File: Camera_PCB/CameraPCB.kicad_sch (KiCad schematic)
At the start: 0 parts

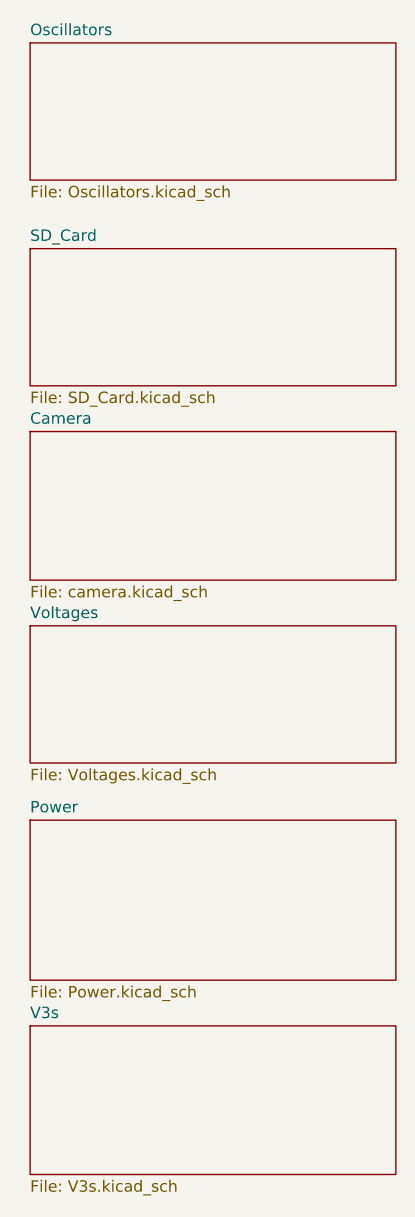
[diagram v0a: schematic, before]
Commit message: 10/29 Footprint Additions
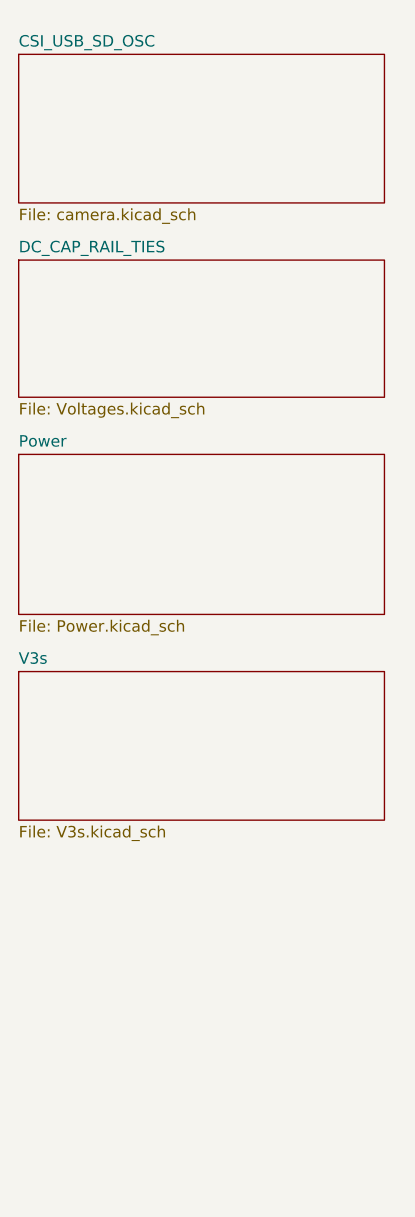
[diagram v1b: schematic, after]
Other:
- sheet Camera renamed CSI_USB_SD_OSC
- sheet Voltages renamed DC_CAP_RAIL_TIES
- removed sheet Oscillators
- removed sheet SD_Card
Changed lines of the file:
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@@
 	)
 	(sheet
-		(at 17.78 60.96)
+		(at 16.51 19.05)
 		(size 40.64 16.51)
 		(exclude_from_sim no)
@@
 			(color 0 0 0 0.0000)
 		)
-		(property "Sheetname" "Camera"
-			(at 17.78 60.2484 0)
+		(property "Sheetname" "CSI_USB_SD_OSC"
+			(at 16.51 18.3384 0)
 			(effects
 				(font
@@
 		)
 		(property "Sheetfile" "camera.kicad_sch"
-			(at 17.78 78.0546 0)
+			(at 16.51 36.1446 0)
 			(effects
 				(font
@@
 	)
 	(sheet
-		(at 17.78 127)
+		(at 16.51 87.63)
 		(size 40.64 16.51)
 		(exclude_from_sim no)
@@
 		)
 		(property "Sheetname" "V3s"
-			(at 17.78 126.2884 0)
+			(at 16.51 86.9184 0)
 			(effects
 				(font
@@
 		)
 		(property "Sheetfile" "V3s.kicad_sch"
-			(at 17.78 144.0946 0)
+			(at 16.51 104.7246 0)
 			(effects
 				(font
@@
 	)
 	(sheet
-		(at 17.78 17.78)
-		(size 40.64 15.24)
-		(exclude_from_sim no)
-		(in_bom yes)
-		(on_board yes)
-		(dnp no)
-		(fields_autoplaced yes)
-		(stroke
-			(width 0.1524)
-			(type solid)
-		)
-		(fill
-			(color 0 0 0 0.0000)
-		)
-		(property "Sheetname" "Oscillators"
-			(at 17.78 17.0684 0)
-			(effects
-				(font
-					(size 1.27 1.27)
-				)
-				(justify left bottom)
-			)
-		)
-		(property "Sheetfile" "Oscillators.kicad_sch"
-			(at 17.78 33.6046 0)
-			(effects
-				(font
-					(size 1.27 1.27)
-				)
-				(justify left top)
-			)
-		)
-		(instances
-			(project "CameraPCB"
-				(path "/400c1603-202c-4359-a830-d2f0d06dd3ce"
-					(page "2")
-				)
-			)
-		)
-	)
-	(sheet
-		(at 17.78 104.14)
+		(at 16.51 63.5)
 		(size 40.64 17.78)
 		(exclude_from_sim no)
@@
 		)
 		(property "Sheetname" "Power"
-			(at 17.78 103.4284 0)
+			(at 16.51 62.7884 0)
 			(effects
 				(font
@@
 		)
 		(property "Sheetfile" "Power.kicad_sch"
-			(at 17.78 122.5046 0)
+			(at 16.51 81.8646 0)
 			(effects
 				(font
@@
 	)
 	(sheet
-		(at 17.78 82.55)
+		(at 16.51 41.91)
 		(size 40.64 15.24)
 		(exclude_from_sim no)
@@
 			(color 0 0 0 0.0000)
 		)
-		(property "Sheetname" "Voltages"
-			(at 17.78 81.8384 0)
+		(property "Sheetname" "DC_CAP_RAIL_TIES"
+			(at 16.51 41.1984 0)
 			(effects
 				(font
@@
 		)
 		(property "Sheetfile" "Voltages.kicad_sch"
-			(at 17.78 98.3746 0)
+			(at 16.51 57.7346 0)
 			(effects
 				(font
@@
 				)
 			)
-		)
-	)
-	(sheet
-		(at 17.78 40.64)
-		(size 40.64 15.24)
-		(exclude_from_sim no)
-		(in_bom yes)
-		(on_board yes)
-		(dnp no)
-		(fields_autoplaced yes)
-		(stroke
-			(width 0.1524)
-			(type solid)
-		)
-		(fill
-			(color 0 0 0 0.0000)
-		)
-		(property "Sheetname" "SD_Card"
-			(at 17.78 39.9284 0)
-			(effects
-				(font
-					(size 1.27 1.27)
-				)
-				(justify left bottom)
-			)
-		)
-		(property "Sheetfile" "SD_Card.kicad_sch"
-			(at 17.78 56.4646 0)
-			(effects
-				(font
-					(size 1.27 1.27)
-				)
-				(justify left top)
-			)
-		)
-		(instances
-			(project "CameraPCB"
-				(path "/400c1603-202c-4359-a830-d2f0d06dd3ce"
-					(page "3")
-				)
-			)

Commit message: Camera PCB Schematic review 1
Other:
- sheet Power renamed AXP203
- added sheet 3V3_5V0 (untitled.kicad_sch)
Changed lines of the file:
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@@
 	)
 	(sheet
-		(at 16.51 87.63)
+		(at 16.51 110.49)
 		(size 40.64 16.51)
 		(exclude_from_sim no)
@@
 		)
 		(property "Sheetname" "V3s"
-			(at 16.51 86.9184 0)
+			(at 16.51 109.7784 0)
 			(effects
 				(font
@@
 		)
 		(property "Sheetfile" "V3s.kicad_sch"
-			(at 16.51 104.7246 0)
+			(at 16.51 127.5846 0)
 			(effects
 				(font
@@
 			(color 0 0 0 0.0000)
 		)
-		(property "Sheetname" "Power"
+		(property "Sheetname" "AXP203"
 			(at 16.51 62.7884 0)
 			(effects
@@
 				)
 			)
+		)
+	)
+	(sheet
+		(at 16.51 87.63)
+		(size 40.64 16.51)
+		(exclude_from_sim no)
+		(in_bom yes)
+		(on_board yes)
+		(dnp no)
+		(fields_autoplaced yes)
+		(stroke
+			(width 0.1524)
+			(type solid)
+		)
+		(fill
+			(color 0 0 0 0.0000)
+		)
+		(property "Sheetname" "3V3_5V0"
+			(at 16.51 86.9184 0)
+			(effects
+				(font
+					(size 1.27 1.27)
+				)
+				(justify left bottom)
+			)
+		)
+		(property "Sheetfile" "untitled.kicad_sch"
+			(at 16.51 104.7246 0)
+			(effects
+				(font
+					(size 1.27 1.27)
+				)
+				(justify left top)
+			)
+		)
+		(instances
+			(project "CameraPCB"
+				(path "/400c1603-202c-4359-a830-d2f0d06dd3ce"
+					(page "6")
+				)
+			)

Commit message: cleaned up Camera_PCB \repository
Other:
- sheet 3V3_5V0: file untitled.kicad_sch -> 3V3_5V0.kicad_sch
- sheet AXP203: file Power.kicad_sch -> AXP203.kicad_sch
- sheet CSI_USB_SD_OSC: file camera.kicad_sch -> CSI_USB_SD_OSC.kicad_sch
- sheet DC_CAP_RAIL_TIES: file Voltages.kicad_sch -> DC_CAP_RAIL_TIES.kicad_sch
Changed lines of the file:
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@@
 			)
 		)
-		(property "Sheetfile" "camera.kicad_sch"
+		(property "Sheetfile" "CSI_USB_SD_OSC.kicad_sch"
 			(at 16.51 36.1446 0)
 			(effects
@@
 			)
 		)
-		(property "Sheetfile" "Power.kicad_sch"
+		(property "Sheetfile" "AXP203.kicad_sch"
 			(at 16.51 81.8646 0)
 			(effects
@@
 			)
 		)
-		(property "Sheetfile" "Voltages.kicad_sch"
+		(property "Sheetfile" "DC_CAP_RAIL_TIES.kicad_sch"
 			(at 16.51 57.7346 0)
 			(effects
@@
 			)
 		)
-		(property "Sheetfile" "untitled.kicad_sch"
+		(property "Sheetfile" "3V3_5V0.kicad_sch"
 			(at 16.51 104.7246 0)
 			(effects
